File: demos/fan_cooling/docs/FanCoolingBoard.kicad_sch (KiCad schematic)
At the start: 7 parts, among them J1 Header1xNFemale, J2 Header1xNFemale, U2 SN74AHC1G14

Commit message: export: kicad_sch — Phase 2.5b: layered placement, wire routing, KiCad 10 compatibility (#23)
* export: kicad_sch — Phase 2.5b: layered placement + routing + KiCad 9 fix

Placement (placement.py, complete rewrite):
- Replaces naive grid with Layered Signal Flow algorithm (spec §5 stages 1–8)
- Stage 1: band classification — power chips/rails at top, LEDs at bottom,
  everything else in the signal band
- Stage 2: signal-flow DAG via BFS from Rail/Connector sources; layer = BFS
  distance from nearest source
- Stage 3–4: place within (band, layer) cells at 1500-mil (38.1 mm) same-band
  spacing, 1000-mil inter-band gutter, 25.4 mm page margin
- Stage 6: cluster breakup — up to 10 iterations shifting same-band parts
  that land closer than 0.9× SAME_BAND_SPACING_MM
- Stage 8: page sized to fit (A4 → A3 → A2 → A1)
- grid_place() and sheet_size_mm() kept as shims for backward-compat

Routing (routing.py, new file):
- route_net(): connects stub ends with Manhattan L-shapes (horizontal first)
- find_junctions(): returns points where ≥3 wire endpoints coincide
- renderer uses routed wires between signal-net stub ends

Hierarchical (hierarchical.py, new file):
- collect_boards(), is_multi_board(), sub_sheet_filename() — interface stub
  for multi-Board sub-sheet emission (full implementation deferred)

KiCad 9 sub-symbol name fix (library_loader.py):
- KiCad 9 schematics expect sub-symbols nested inside their parent in
  lib_symbols to use the bare name (R_0_1, LED_0_1, 4069_1_0) — NOT the
  lib-qualified name (Device:R_0_1, Device:LED_0_1, 4xxx:4069_1_0)
- Fixed _qualify_names() to add the lib: prefix only to the exact parent
  symbol name using a lookahead (?=") that prevents sub-unit names from
  being qualified

Tests (+25 tests):
- test_placement.py: band classification, all-on-grid, determinism,
  minimum spacing, power < signal < indicator Y ordering, page sizing
- test_routing.py: H/V segments, L-shapes, orthogonality, grid snap,
  junction detection

Golden files re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
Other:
- moved on the sheet: D1, J1, J2, R1, R2, R3
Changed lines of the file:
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@@
 (kicad_sch
-  (version 20240618)
+  (version 20250114)
   (generator "wirebench")
-  (generator_version "0.1")
-  (paper "A3")
+  (generator_version "0.2")
+  (paper "A2")
   (symbol
     (lib_id "74xx:74AHC1G14")
-    (at 149.86 30.48 0)
+    (at 63.5 368.3 0)
     (unit 1)
     (exclude_from_sim no)
@@
     (dnp no)
     (property "Reference" "U2"
-      (at 152.4 27.94 0)
+      (at 66.04 365.76 0)
       (effects (font (size 1.27 1.27)))
     )
     (property "Value" "SN74AHC1G14"
-      (at 149.86 33.02 0)
+      (at 63.5 370.84 0)
       (effects (font (size 1.27 1.27)))
     )
@@
   (symbol
     (lib_id "Device:D_Zener")
-    (at 229.87 30.48 0)
+    (at 63.5 25.4 0)
     (unit 1)
     (exclude_from_sim no)
@@
     (dnp no)
     (property "Reference" "D1"
-      (at 232.41 27.94 0)
+      (at 66.04 22.86 0)
       (effects (font (size 1.27 1.27)))
     )
     (property "Value" "1N4728A"
-      (at 229.87 33.02 0)
-      (effects (font (size 1.27 1.27)))
-    )
-    (pin "1")
-    (pin "2")
-  )
-  (wire
-    (pts (xy 226.06 30.48) (xy 223.52 30.48))
-    (stroke (width 0) (type default))
-  )
-  (wire
-    (pts (xy 233.68 30.48) (xy 236.22 30.48))
+      (at 63.5 27.94 0)
+      (effects (font (size 1.27 1.27)))
+    )
+    (pin "1")
+    (pin "2")
+  )
+  (wire
+    (pts (xy 59.69 25.4) (xy 57.15 25.4))
+    (stroke (width 0) (type default))
+  )
+  (wire
+    (pts (xy 67.31 25.4) (xy 69.85 25.4))
     (stroke (width 0) (type default))
   )
   (symbol
     (lib_id "Device:R")
-    (at 30.48 69.85 0)
+    (at 63.5 215.9 0)
     (unit 1)
     (exclude_from_sim no)
@@
     (dnp no)
     (property "Reference" "R1"
-      (at 33.02 67.31 0)
+      (at 66.04 213.36 0)
       (effects (font (size 1.27 1.27)))
     )
     (property "Value" "1e+04 Ω"
-      (at 30.48 72.39 0)
-      (effects (font (size 1.27 1.27)))
-    )
-    (pin "1")
-    (pin "2")
-  )
-  (wire
-    (pts (xy 30.48 73.66) (xy 30.48 76.2))
-    (stroke (width 0) (type default))
-  )
-  (wire
-    (pts (xy 30.48 66.04) (xy 30.48 63.5))
+      (at 63.5 218.44 0)
+      (effects (font (size 1.27 1.27)))
+    )
+    (pin "1")
+    (pin "2")
+  )
+  (wire
+    (pts (xy 63.5 219.71) (xy 63.5 222.25))
+    (stroke (width 0) (type default))
+  )
+  (wire
+    (pts (xy 63.5 212.09) (xy 63.5 209.55))
     (stroke (width 0) (type default))
   )
   (symbol
     (lib_id "Device:R")
-    (at 69.85 69.85 0)
+    (at 63.5 254 0)
     (unit 1)
     (exclude_from_sim no)
@@
     (dnp no)
     (property "Reference" "R2"
-      (at 72.39 67.31 0)
+      (at 66.04 251.46 0)
       (effects (font (size 1.27 1.27)))
     )
     (property "Value" "1e+04 Ω"
-      (at 69.85 72.39 0)
-      (effects (font (size 1.27 1.27)))
-    )
-    (pin "1")
-    (pin "2")
-  )
-  (wire
-    (pts (xy 69.85 73.66) (xy 69.85 76.2))
-    (stroke (width 0) (type default))
-  )
-  (wire
-    (pts (xy 69.85 66.04) (xy 69.85 63.5))
+      (at 63.5 256.54 0)
+      (effects (font (size 1.27 1.27)))
+    )
+    (pin "1")
+    (pin "2")
+  )
+  (wire
+    (pts (xy 63.5 257.81) (xy 63.5 260.35))
+    (stroke (width 0) (type default))
+  )
+  (wire
+    (pts (xy 63.5 250.19) (xy 63.5 247.65))
     (stroke (width 0) (type default))
   )
   (symbol
     (lib_id "Device:R")
-    (at 110.49 69.85 0)
+    (at 63.5 292.1 0)
     (unit 1)
     (exclude_from_sim no)
@@
     (dnp no)
     (property "Reference" "R3"
-      (at 113.03 67.31 0)
+      (at 66.04 289.56 0)
       (effects (font (size 1.27 1.27)))
     )
     (property "Value" "1e+04 Ω"
-      (at 110.49 72.39 0)
-      (effects (font (size 1.27 1.27)))
-    )
-    (pin "1")
-    (pin "2")
-  )
-  (wire
-    (pts (xy 110.49 73.66) (xy 110.49 76.2))
-    (stroke (width 0) (type default))
-  )
-  (wire
-    (pts (xy 110.49 66.04) (xy 110.49 63.5))
+      (at 63.5 294.64 0)
+      (effects (font (size 1.27 1.27)))
+    )
+    (pin "1")
+    (pin "2")
+  )
+  (wire
+    (pts (xy 63.5 295.91) (xy 63.5 298.45))
+    (stroke (width 0) (type default))
+  )
+  (wire
+    (pts (xy 63.5 288.29) (xy 63.5 285.75))
     (stroke (width 0) (type default))
   )
   (symbol
     (lib_id "Connector_Generic:Conn_01x04")
-    (at 149.86 69.85 0)
+    (at 25.4 25.4 0)
     (unit 1)
     (exclude_from_sim no)
@@
     (dnp no)
     (property "Reference" "J1"
-      (at 152.4 67.31 0)
+      (at 27.94 22.86 0)
       (effects (font (size 1.27 1.27)))
     )
     (property "Value" "Header1xNFemale"
-      (at 149.86 72.39 0)
+      (at 25.4 27.94 0)
       (effects (font (size 1.27 1.27)))
     )
@@
   )
   (wire
-    (pts (xy 144.78 72.39) (xy 142.24 72.39))
-    (stroke (width 0) (type default))
-  )
-  (wire
-    (pts (xy 144.78 69.85) (xy 142.24 69.85))
-    (stroke (width 0) (type default))
-  )
-  (wire
-    (pts (xy 144.78 67.31) (xy 142.24 67.31))
-    (stroke (width 0) (type default))
-  )
-  (wire
-    (pts (xy 144.78 64.77) (xy 142.24 64.77))
+    (pts (xy 20.32 27.94) (xy 17.78 27.94))
+    (stroke (width 0) (type default))
+  )
+  (wire
+    (pts (xy 20.32 25.4) (xy 17.78 25.4))
+    (stroke (width 0) (type default))
+  )
+  (wire
+    (pts (xy 20.32 22.86) (xy 17.78 22.86))
+    (stroke (width 0) (type default))
+  )
+  (wire
+    (pts (xy 20.32 20.32) (xy 17.78 20.32))
     (stroke (width 0) (type default))
   )
   (symbol
     (lib_id "Connector_Generic:Conn_01x04")
-    (at 190.5 69.85 0)
+    (at 25.4 63.5 0)
     (unit 1)
     (exclude_from_sim no)
@@
     (dnp no)
     (property "Reference" "J2"
-      (at 193.04 67.31 0)
+      (at 27.94 60.96 0)
       (effects (font (size 1.27 1.27)))
     )
     (property "Value" "Header1xNFemale"
-      (at 190.5 72.39 0)
+      (at 25.4 66.04 0)
       (effects (font (size 1.27 1.27)))
     )
@@
   )
   (wire
-    (pts (xy 185.42 72.39) (xy 182.88 72.39))
-    (stroke (width 0) (type default))
-  )
-  (wire
-    (pts (xy 185.42 69.85) (xy 182.88 69.85))
-    (stroke (width 0) (type default))
-  )
-  (wire
-    (pts (xy 185.42 67.31) (xy 182.88 67.31))
-    (stroke (width 0) (type default))
-  )
-  (wire
-    (pts (xy 185.42 64.77) (xy 182.88 64.77))
-    (stroke (width 0) (type default))
-  )
+    (pts (xy 20.32 66.04) (xy 17.78 66.04))
+    (stroke (width 0) (type default))
+  )
+  (wire
+    (pts (xy 20.32 63.5) (xy 17.78 63.5))
+    (stroke (width 0) (type default))
+  )
+  (wire
+    (pts (xy 20.32 60.96) (xy 17.78 60.96))
+    (stroke (width 0) (type default))
+  )
+  (wire
+    (pts (xy 20.32 58.42) (xy 17.78 58.42))
+    (stroke (width 0) (type default))
+  )

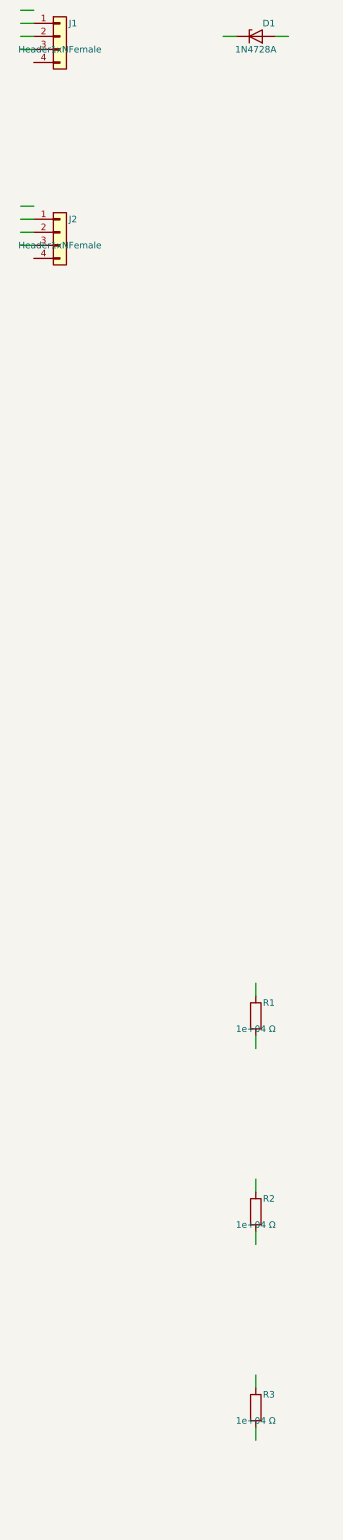
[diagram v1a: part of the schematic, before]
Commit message: framework: passive + diode terminals mandatory (#30)
Continuation of the LED.cathode regression fix (#29). Resistor,
Capacitor, Inductor, and every Diode subclass had their terminals
declared `mandatory=False` with the same "structurally inert under
graph evaluation" justification — letting demos declare BOM-only
timing / decoupling / pull-up parts without wiring them, then ship
breadboard SVGs and netlists where those parts sat orphaned.

A real resistor / capacitor / inductor / diode with a dangling
terminal does nothing. Marking the ports mandatory closes the
silent regression at the framework layer.

  - `src/components/passives/{resistor,capacitor,inductor}.py` and
    every diode subclass under `src/components/diodes/` now declare
    their terminals `mandatory=True`.
  - `tests/components/test_{resistor,capacitor,inductor}.py`:
    regression tests pin the new contract per component.
  - `tests/components/test_diode_mandatory_terminals.py` (new):
    parametrized over D1N4001 / D1N4007 / D1N4148 / D1N4728A /
    D1N4733A / D1N4742A / D1N5817.
  - Six demos (`backup_power`, `bldc_motor`, `dice`,
    `doorbell_protector`, `fan_cooling`, `isolated_rs232`) had
    declared-but-unwired passives — each now wires them either to
    their datasheet-correct net (e.g. DoorbellProtector's flyback
    diode anode joins the relay coil_minus net) or as an isolated
    0-Ω passthrough with `dynamically_driven=True` where the part
    is genuinely BOM-only and the voltage-only simulator can't
    honour its behaviour. Comments at each call site explain
    which kind.
  - Test fixtures across CLI, refdes, format-roundtrip, kicad
    import, and per-format renderer tests updated so they still
    pin down the specific error each one exists to catch without
    tripping the new mandatory-pin check first.
  - All demo docs regenerated; goldens refreshed.

After this commit the breadboard SVGs show every BOM part connected
to something — no more orphaned caps and resistors float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
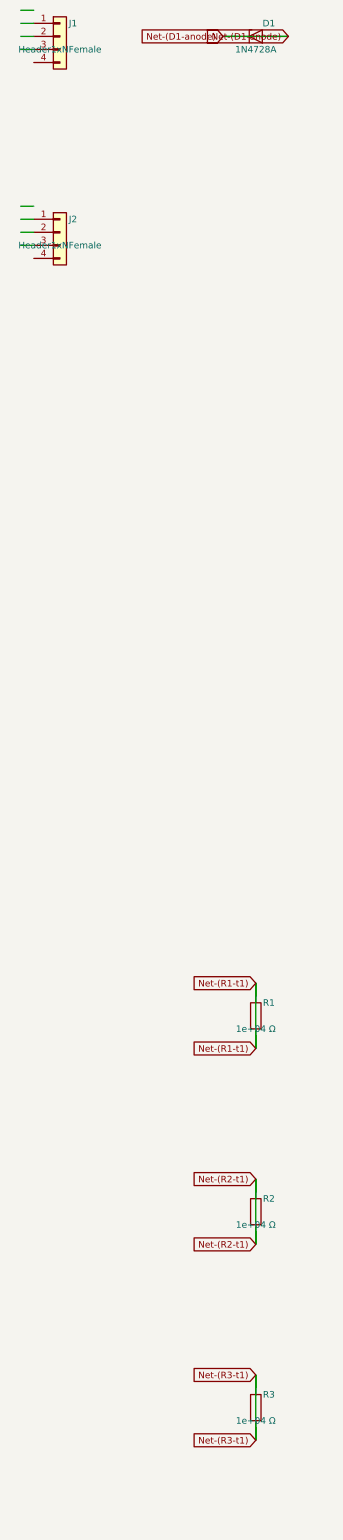
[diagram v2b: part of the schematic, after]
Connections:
- net Net-(D1-anode): now reaches D1.1 (K)
- net Net-(D1-anode): now also D1.2 (A)
- net Net-(R3-t1): now reaches R3.1
- net Net-(R3-t1): now also R3.2
- net Net-(R2-t1): now reaches R2.1
- net Net-(R2-t1): now also R2.2
- net Net-(R1-t1): now reaches R1.1
- net Net-(R1-t1): now also R1.2
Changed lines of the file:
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@@
     (stroke (width 0) (type default))
+  )
+  (global_label "Net-(D1-anode)"
+    (shape input)
+    (at 57.15 25.4 0)
+    (fields_autoplaced yes)
+    (effects (font (size 1.27 1.27)) (justify right))
+    (property "Intersheet References" "${INTERSHEET_REFS}"
+      (at 0 0 0)
+      (effects (font (size 1.27 1.27)) (hide yes))
+    )
   )
   (wire
     (pts (xy 67.31 25.4) (xy 69.85 25.4))
     (stroke (width 0) (type default))
+  )
+  (global_label "Net-(D1-anode)"
+    (shape input)
+    (at 69.85 25.4 0)
+    (fields_autoplaced yes)
+    (effects (font (size 1.27 1.27)) (justify right))
+    (property "Intersheet References" "${INTERSHEET_REFS}"
+      (at 0 0 0)
+      (effects (font (size 1.27 1.27)) (hide yes))
+    )
   )
   (symbol
@@
     (stroke (width 0) (type default))
   )
+  (global_label "Net-(R1-t1)"
+    (shape input)
+    (at 63.5 222.25 0)
+    (fields_autoplaced yes)
+    (effects (font (size 1.27 1.27)) (justify right))
+    (property "Intersheet References" "${INTERSHEET_REFS}"
+      (at 0 0 0)
+      (effects (font (size 1.27 1.27)) (hide yes))
+    )
+  )
   (wire
     (pts (xy 63.5 212.09) (xy 63.5 209.55))
     (stroke (width 0) (type default))
+  )
+  (global_label "Net-(R1-t1)"
+    (shape input)
+    (at 63.5 209.55 0)
+    (fields_autoplaced yes)
+    (effects (font (size 1.27 1.27)) (justify right))
+    (property "Intersheet References" "${INTERSHEET_REFS}"
+      (at 0 0 0)
+      (effects (font (size 1.27 1.27)) (hide yes))
+    )
   )
   (symbol
@@
     (stroke (width 0) (type default))
   )
+  (global_label "Net-(R2-t1)"
+    (shape input)
+    (at 63.5 260.35 0)
+    (fields_autoplaced yes)
+    (effects (font (size 1.27 1.27)) (justify right))
+    (property "Intersheet References" "${INTERSHEET_REFS}"
+      (at 0 0 0)
+      (effects (font (size 1.27 1.27)) (hide yes))
+    )
+  )
   (wire
     (pts (xy 63.5 250.19) (xy 63.5 247.65))
     (stroke (width 0) (type default))
+  )
+  (global_label "Net-(R2-t1)"
+    (shape input)
+    (at 63.5 247.65 0)
+    (fields_autoplaced yes)
+    (effects (font (size 1.27 1.27)) (justify right))
+    (property "Intersheet References" "${INTERSHEET_REFS}"
+      (at 0 0 0)
+      (effects (font (size 1.27 1.27)) (hide yes))
+    )
   )
   (symbol
@@
     (stroke (width 0) (type default))
   )
+  (global_label "Net-(R3-t1)"
+    (shape input)
+    (at 63.5 298.45 0)
+    (fields_autoplaced yes)
+    (effects (font (size 1.27 1.27)) (justify right))
+    (property "Intersheet References" "${INTERSHEET_REFS}"
+      (at 0 0 0)
+      (effects (font (size 1.27 1.27)) (hide yes))
+    )
+  )
   (wire
     (pts (xy 63.5 288.29) (xy 63.5 285.75))
     (stroke (width 0) (type default))
+  )
+  (global_label "Net-(R3-t1)"
+    (shape input)
+    (at 63.5 285.75 0)
+    (fields_autoplaced yes)
+    (effects (font (size 1.27 1.27)) (justify right))
+    (property "Intersheet References" "${INTERSHEET_REFS}"
+      (at 0 0 0)
+      (effects (font (size 1.27 1.27)) (hide yes))
+    )
   )
   (symbol
@@
     (stroke (width 0) (type default))
   )
+  (wire
+    (pts (xy 57.15 25.4) (xy 69.85 25.4))
+    (stroke (width 0) (type default))
+  )
+  (wire
+    (pts (xy 63.5 209.55) (xy 63.5 222.25))
+    (stroke (width 0) (type default))
+  )
+  (wire
+    (pts (xy 63.5 247.65) (xy 63.5 260.35))
+    (stroke (width 0) (type default))
+  )
+  (wire
+    (pts (xy 63.5 285.75) (xy 63.5 298.45))
+    (stroke (width 0) (type default))
+  )

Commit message: units: Ohms.__str__ uses engineering notation (kΩ, MΩ, GΩ)
The previous `Ohms.__str__` formatted with bare `:.3g`, producing
unreadable scientific output for clean kilo / mega multiples:

  str(Ohms(10_000))     == "1e+04 Ω"      → now "10 kΩ"
  str(Ohms(100_000))    == "1e+05 Ω"      → now "100 kΩ"
  str(Ohms(1_000_000))  == "1e+06 Ω"      → now "1 MΩ"

The breadboard SVG visualiser surfaced the problem: a resistor body
labelled "100000Ω" makes a reader count zeros, while a label of
"100 kΩ" reads at a glance — exactly the convention every schematic
and parts catalogue uses. Centralising the engineering notation in
`Ohms.__str__` means every downstream consumer (assembly guide,
breadboard SVG, kicad netlist, BOM, reports) inherits the readable
form without each format adapter rolling its own formatter.

  - `Ohms.__str__` returns "47 Ω", "4.7 kΩ", "10 kΩ", "100 kΩ",
    "1 MΩ", "10 MΩ", "1 GΩ" per the kilo / mega / giga thresholds.
  - `Resistor.__str__` delegates to `str(self._ohms)` so it
    inherits the new notation (was producing the noisy "47.0 Ω"
    via raw float).
  - The breadboard visualiser's resistor body label uses
    `str(part.ohms)` directly (previously had a private
    `_format_ohms_compact` helper; removed).
  - `tests/components/test_resistor.py::test_str` updated for
    "47 Ω" (was "47.0 Ω"); new `test_str_renders_in_engineering_notation`
    pins kΩ / MΩ output across the kilo and mega thresholds.
  - All demo docs / goldens refreshed where the Ohms.__str__
    change affected the rendered output (breadboard SVGs, kicad
    sch value fields, BOM rows).
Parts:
- R1, R2, R3: value 1e+04 Ω -> 10 kΩ
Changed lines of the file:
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@@
       (effects (font (size 1.27 1.27)))
     )
-    (property "Value" "1e+04 Ω"
+    (property "Value" "10 kΩ"
       (at 63.5 218.44 0)
       (effects (font (size 1.27 1.27)))
@@
       (effects (font (size 1.27 1.27)))
     )
-    (property "Value" "1e+04 Ω"
+    (property "Value" "10 kΩ"
       (at 63.5 256.54 0)
       (effects (font (size 1.27 1.27)))
@@
       (effects (font (size 1.27 1.27)))
     )
-    (property "Value" "1e+04 Ω"
+    (property "Value" "10 kΩ"
       (at 63.5 294.64 0)
       (effects (font (size 1.27 1.27)))
